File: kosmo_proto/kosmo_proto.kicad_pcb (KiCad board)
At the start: 2 copper layers, 100.3 x 55.9 mm, 565 parts, among them J9901 Conn_01x01, J9902 Conn_01x01, J9903 Conn_01x01, J9904 Conn_01x01, J9905 Conn_01x01, J9906 Conn_01x01, J9907 EURO_PWR_2x5

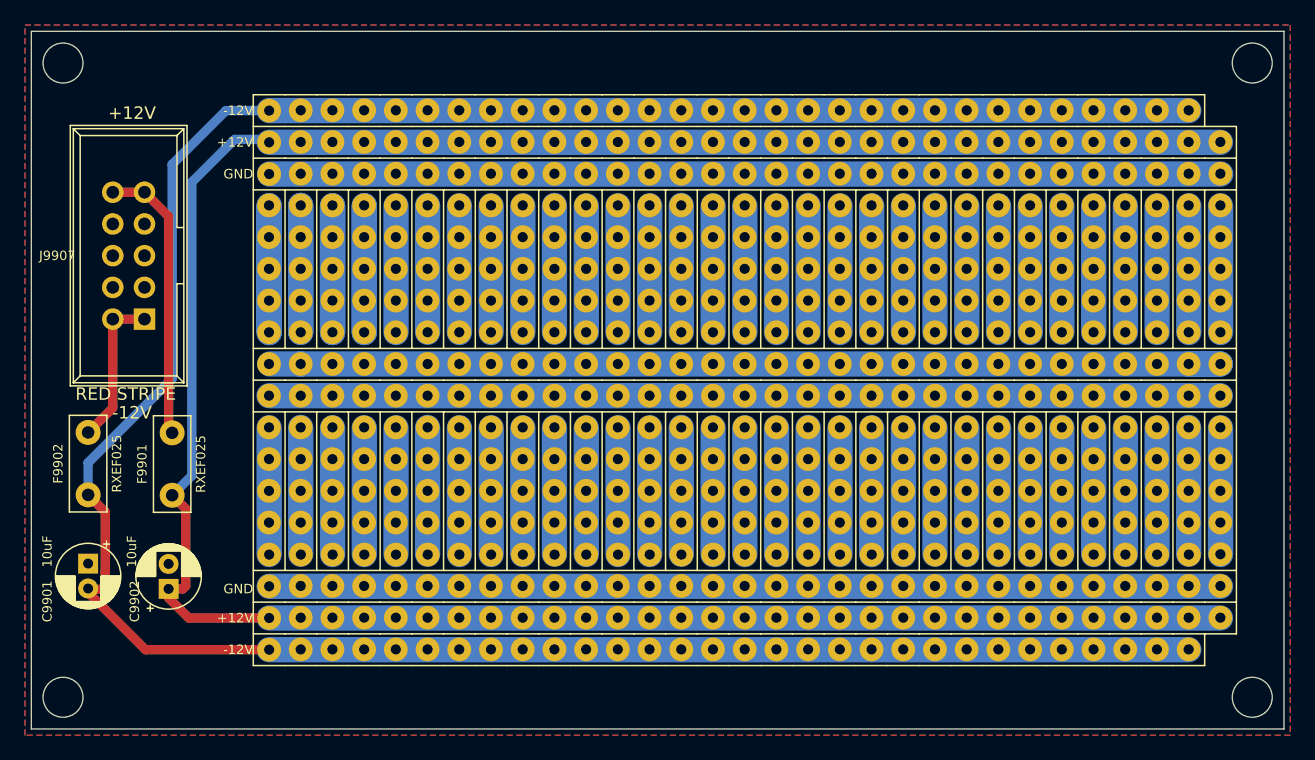
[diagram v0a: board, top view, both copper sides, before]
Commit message: Replace fuses with diodes; improve layout; add row/column identifiers
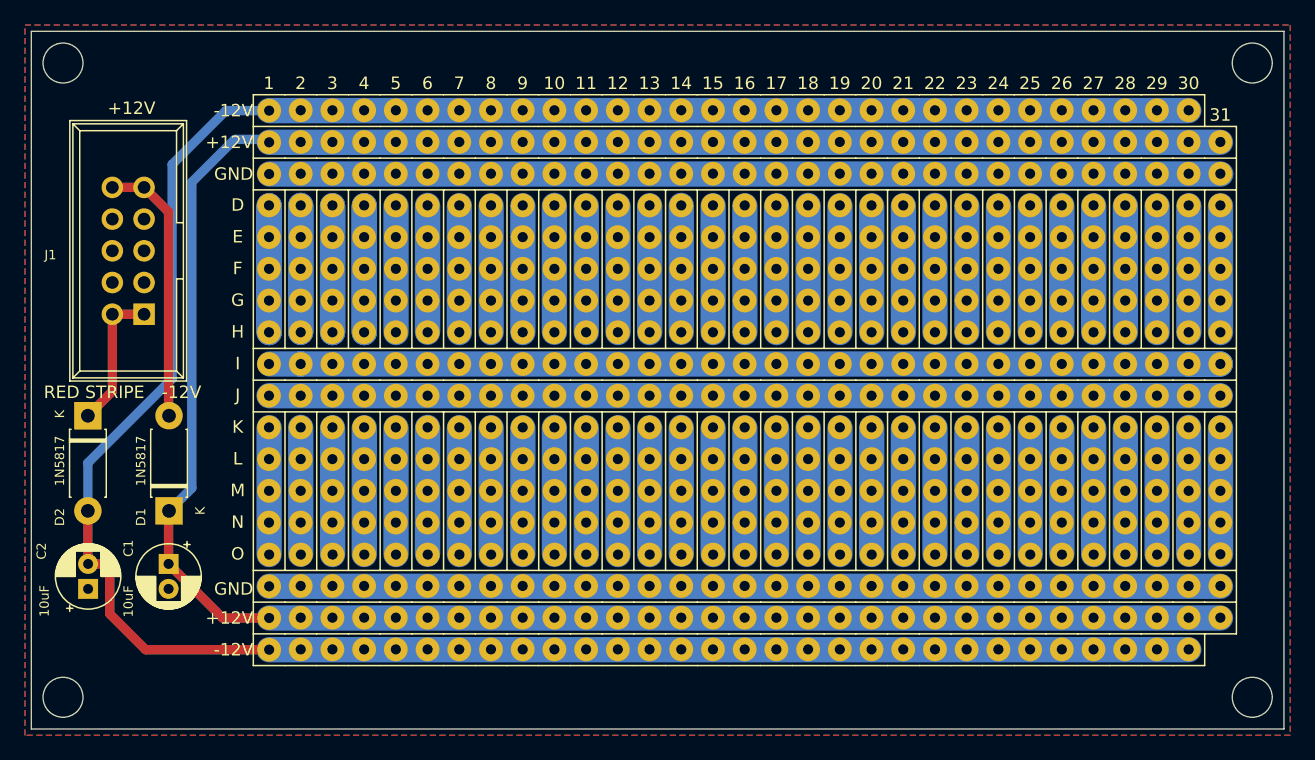
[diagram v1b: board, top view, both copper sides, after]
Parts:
- removed C9902: 10uF, ao_tht:CP_Radial_D5.0mm_P2.00mm
- removed F9901, F9902: RXEF025, ao_tht:PPTC_RXEF025
- removed J9907: EURO_PWR_2x5, ao_tht:Power_Header
- added C2: 10uF, ao_tht:CP_Radial_D5.0mm_P2.00mm, F.Cu at (50.3, 98.0)
- added D1: 1N5817, ao_tht:D_DO-41_SOD81_P7.62mm_Horizontal, F.Cu at (56.8, 91.8)
- added D2: 1N5817, ao_tht:D_DO-41_SOD81_P7.62mm_Horizontal, F.Cu at (50.2, 84.1)
- added J1: Synth_power_2x5, ao_tht:Power_Header, F.Cu at (54.8, 76.0)
- moved C1 2.00 mm to (56.7, 96.0), turned to 270 degrees
- renumbered C9901 to C1, J9901 to J2, J9904 to J3, J9902 to J4, J9905 to J5, J9903 to J6, J9906 to J7
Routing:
- net Net-(F9901-Pad2): track 22.6 -> 0.00 mm
- net Net-(D1-Pad2): track 0.00 -> 21.7 mm
- net Net-(F9902-Pad2): track 12.4 -> 0.00 mm
- net Net-(D2-Pad1): track 0.00 -> 11.5 mm
- net +12V: track 205.0 -> 201.3 mm
- net -12V: track 212.3 -> 211.0 mm
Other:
- board text added: "1"
- board text added: "10"
- board text added: "11"
- board text added: "12"
- board text added: "13"
- board text added: "14"
- board text added: "15"
- board text added: "16"
- board text added: "17"
- board text added: "18"
- board text added: "19"
- board text added: "2"
- board text added: "20"
- board text added: "21"
- board text added: "22"
- board text added: "23"
- board text added: "24"
- board text added: "25"
- board text added: "26"
- board text added: "27"
- board text added: "28"
- board text added: "29"
- board text added: "3"
- board text added: "30"
- board text added: "31"
- board text added: "4"
- board text added: "5"
- board text added: "6"
- board text added: "7"
- board text added: "8"
- board text added: "9"
- board text added: "D"
- board text added: "E"
- board text added: "F"
- board text added: "G"
- board text added: "H"
- board text added: "I"
- board text added: "J"
- board text added: "K"
- board text added: "L"
- board text added: "M"
- board text added: "N"
- board text added: "O"

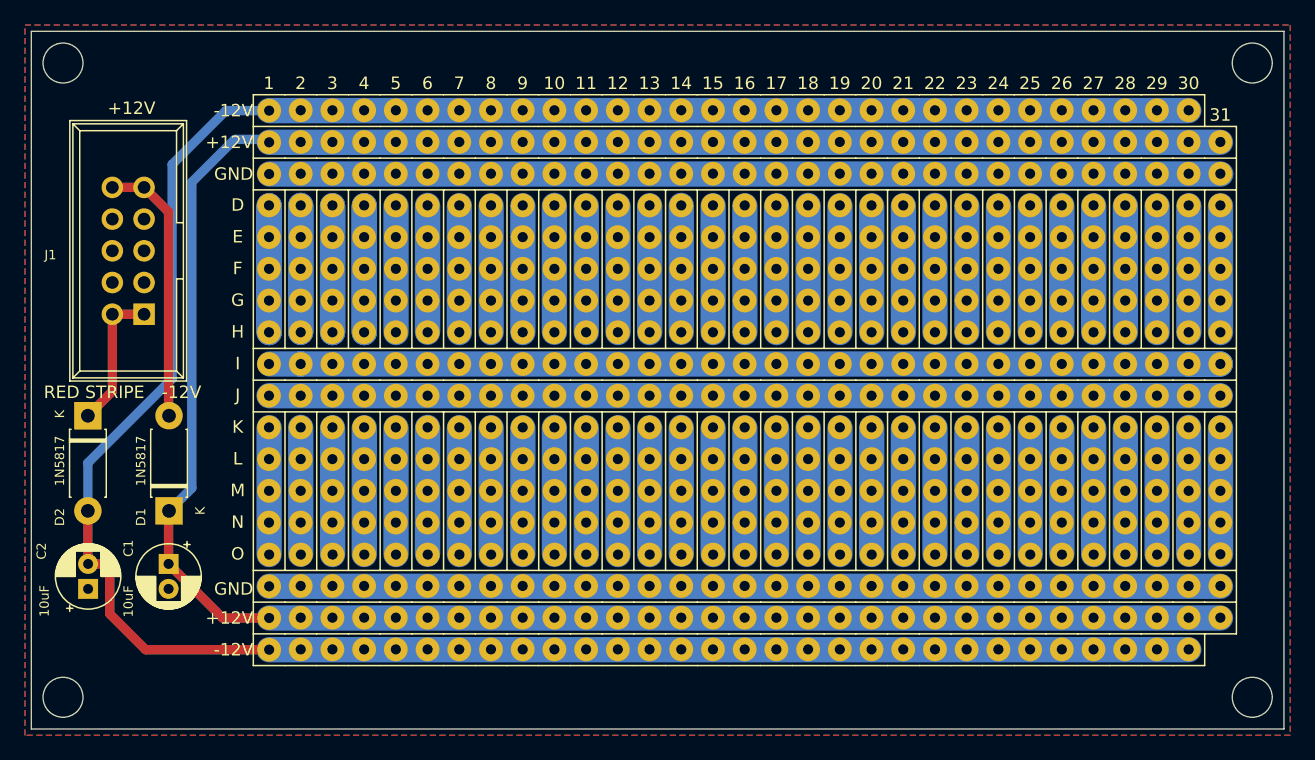
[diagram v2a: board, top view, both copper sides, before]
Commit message: Dupe numbers and letters; add text/logo; change cap footprints; size and positioning tweaks
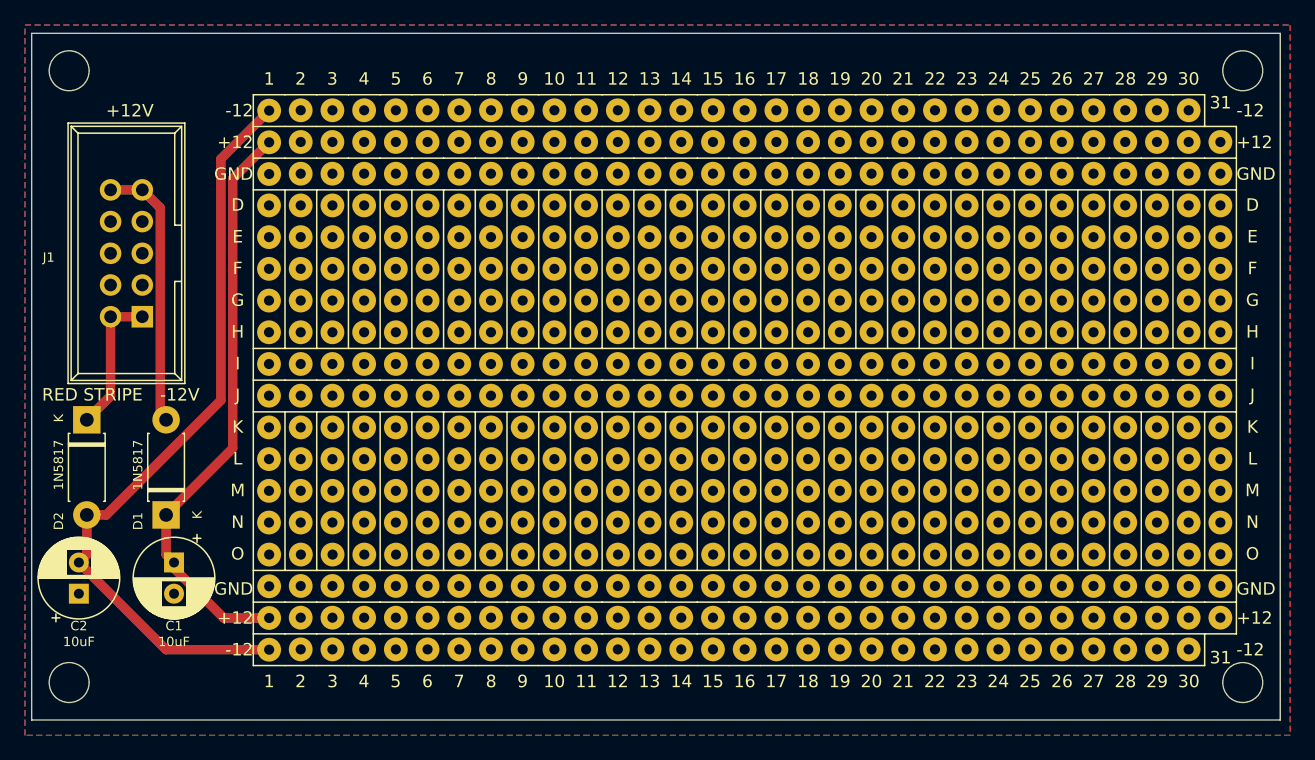
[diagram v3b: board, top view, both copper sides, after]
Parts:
- removed the REF** at (143.5, 106.7)
- removed the REF** at (143.5, 55.9)
- added GRAF1: AO logo, ao_tht:analogoutput_12mm, B.Cu at (57.1, 59.7)
- added GRAF2: CC0 logo, ao_tht:CC0_logo, B.Cu at (87.6, 106.0)
- added REF**: MountingHole_3.2mm_M3, ao_tht:MountingHole_3.2mm_M3, F.Cu at (142.8, 56.5)
- added REF**: MountingHole_3.2mm_M3, ao_tht:MountingHole_3.2mm_M3, F.Cu at (142.8, 105.5)
- C1, C2: footprint ao_tht:CP_Radial_D5.0mm_P2.00mm -> ao_tht:CP_Radial_D6.3mm_P2.50mm
- moved REF** 1.28 mm to (48.8, 105.5)
- moved C2 0.83 mm to (49.5, 98.4)
- moved REF** 0.79 mm to (48.8, 56.5)
- moved C1 0.45 mm to (57.1, 95.9)
- moved D1 0.40 mm to (56.5, 92.1)
- moved D2 0.34 mm to (50.2, 84.5)
- moved J1 0.24 mm to (54.6, 76.2)
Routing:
- net (no net): track 825.4 -> 0.00 mm
- net +12V: track 201.3 -> 47.1 mm
- net GND: track 152.4 -> 0.00 mm
- net -12V: track 211.0 -> 61.6 mm
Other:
- board size 100.3 x 55.9 mm -> 100 x 55 mm
- net class Default: trace_width 0.25 -> 0.75
- board text added: "+12"
- board text added: "-12"
- board text added: "Euro/Kosmo Protoboard"
- board text added: "Rich Holmes / CC0 1.0"
- board text removed: "+12V"
- board text removed: "-12V"

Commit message: pcb tweak
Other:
- rule pad_to_mask_clearance: 0.051 -> 0
